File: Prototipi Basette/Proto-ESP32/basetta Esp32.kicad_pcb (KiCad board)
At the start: 2 copper layers, 71.1 x 68.3 mm, 26 parts, among them J1 Conn_01x19, J2 Conn_01x19, J3 Conn_01x19, J4 Conn_01x19, J5 Screw_Terminal_01x02, J6 Conn_01x05, Q1 BC547, Q2 BC547, Q3 IRF9540N, SW1 RESET, SW2 SET, U3 4013

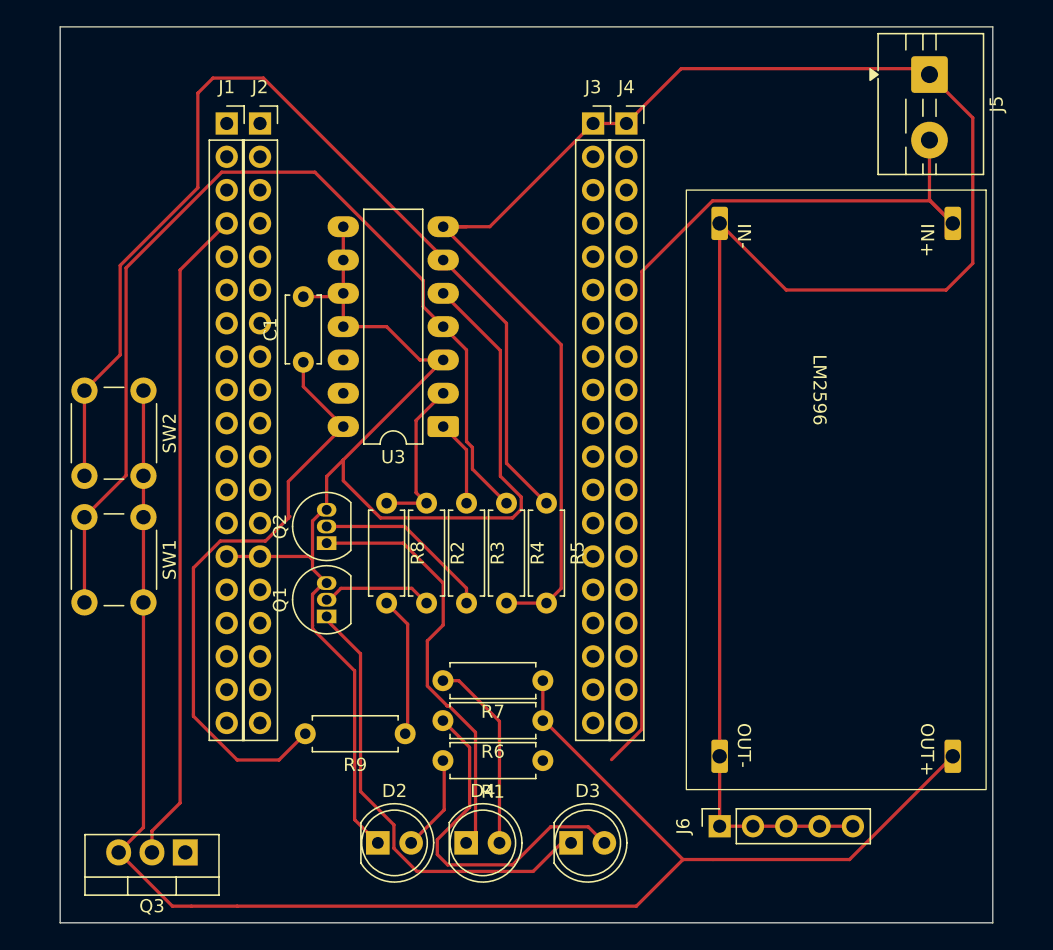
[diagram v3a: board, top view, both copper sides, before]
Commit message: Modifica PCB - Parallelo Suicide
Aggiunto comando suicide da ESP32
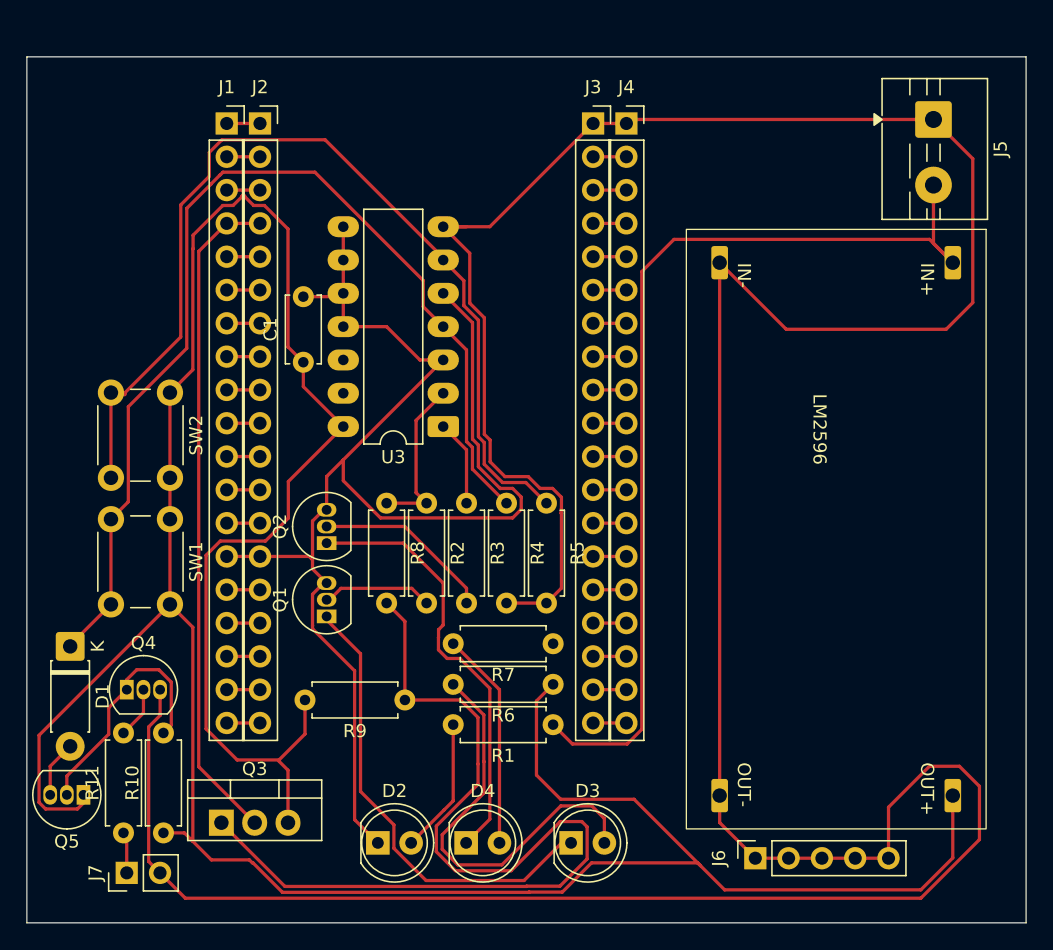
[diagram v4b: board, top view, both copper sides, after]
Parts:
- added D1: 1N4007, Diode_THT:D_DO-41_SOD81_P7.62mm_Horizontal, F.Cu at (127.8, 100.8)
- added J7: Conn_01x02, Connector_PinHeader_2.54mm:PinHeader_1x02_P2.54mm_Vertical, F.Cu at (132.1, 118.1)
- added Q4: BC547, Package_TO_SOT_THT:TO-92_Inline, F.Cu at (132.1, 104.1)
- added Q5: BC557, Package_TO_SOT_THT:TO-92_Inline, F.Cu at (128.8, 112.2)
- added R10: R, Resistor_THT:R_Axial_DIN0207_L6.3mm_D2.5mm_P7.62mm_Horizontal, F.Cu at (134.9, 115.1)
- added R11: R, Resistor_THT:R_Axial_DIN0207_L6.3mm_D2.5mm_P7.62mm_Horizontal, F.Cu at (131.8, 115.1)
- moved J6 3.65 mm to (180.0, 117.0)
- moved Q3 3.57 mm to (139.3, 114.3), turned to 0 degrees
- moved J5 3.44 mm to (193.6, 60.7)
- moved LM2596 3.00 mm to (177.3, 71.6)
- moved R7 2.92 mm to (164.6, 100.6)
- moved R6 2.87 mm to (164.6, 103.7)
- moved R1 2.85 mm to (164.6, 106.8)
- moved R9 2.57 mm to (153.3, 104.9)
- moved SW1 2.03 mm to (135.4, 91.1)
- moved SW2 2.03 mm to (135.4, 81.5)
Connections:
- net 5 V renamed +5V
- net Net-(U3A-R) renamed Suicide
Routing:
- net GND: track 281.0 -> 378.6 mm
- net +5V: track 170.5 -> 236.9 mm
- net Net-(Q3-G): track 10.9 -> 72.6 mm
- net Net-(Q4-C): track 0.00 -> 18.9 mm
- net Net-(U3A-S): track 79.6 -> 73.7 mm
- net Net-(D3-A): track 26.8 -> 31.8 mm
- net Suicide: track 75.5 -> 79.9 mm
- net Net-(D1-A): track 0.00 -> 4.34 mm
- net Net-(Q4-B): track 0.00 -> 3.93 mm
- net Net-(J7-Pin_1): track 0.00 -> 3.15 mm
- net Net-(D2-A): track 7.36 -> 10.3 mm
- net V_in_Batterie: track 71.9 -> 74.7 mm
- net Net-(J3-Pin_9): track 0.00 -> 2.54 mm
- net Net-(J3-Pin_8): track 0.00 -> 2.54 mm
- net Net-(J3-Pin_7): track 0.00 -> 2.54 mm
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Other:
- board size 71.1 x 68.3 mm -> 76.2 x 66 mm

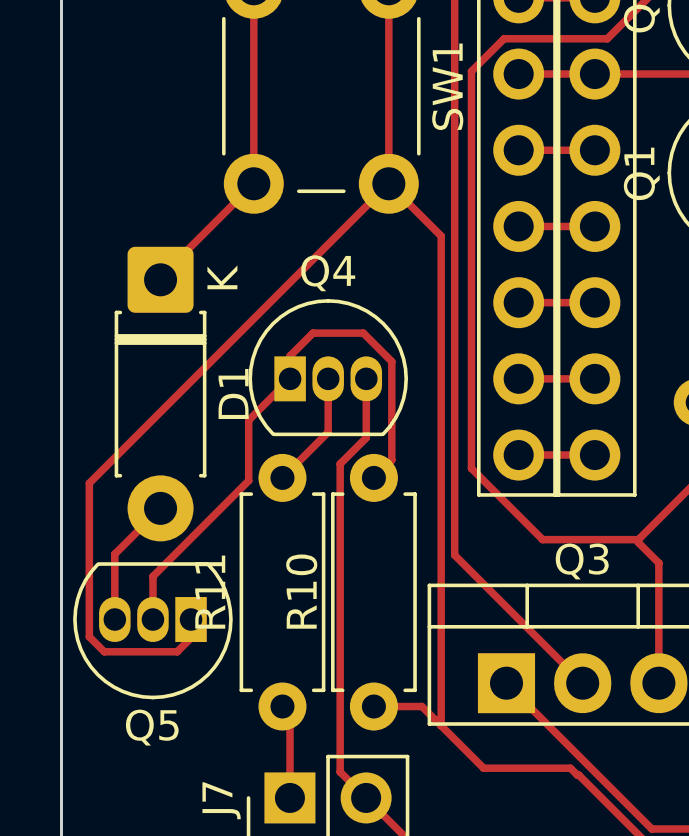
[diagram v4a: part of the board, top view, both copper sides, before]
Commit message: Add Primo Circuito KiCad project; update ESP32 PCB
Add a new KiCad project "Primo Circuito KiCad": schematic (.kicad_sch), board file (.kicad_pcb), project/settings (.kicad_pro, .kicad_prl) and a PDF export (BERNARDIS.pdf). The schematic contains a simple BJT/LED prototype and power symbols. Also update Proto-ESP32: add Basetta_ESP32.zip and a dated backup under basetta Esp32-backups/, remove Gerber.zip, and apply updates to basetta Esp32 KiCad files (.kicad_pcb, .kicad_prl, .kicad_pro, .kicad_sch).
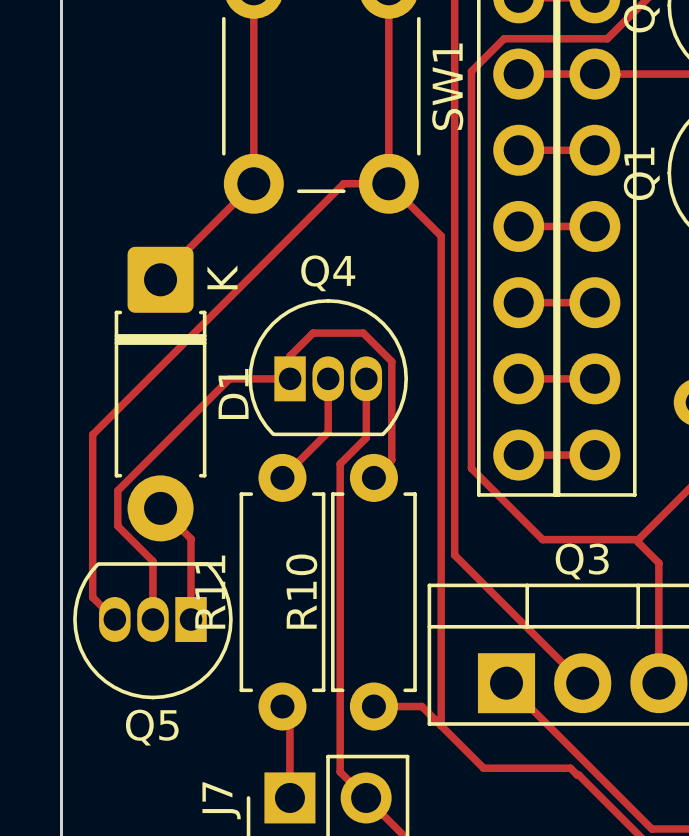
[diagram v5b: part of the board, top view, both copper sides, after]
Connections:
- Q5 pad 1: +5V -> Net-(D1-A)
- Q5 pad 3: Net-(D1-A) -> +5V
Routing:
- net +5V: track 236.9 -> 233.1 mm
- net Net-(Q4-C): track 18.9 -> 21.1 mm
